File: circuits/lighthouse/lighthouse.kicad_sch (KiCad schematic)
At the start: 5 parts, among them U1 ESP32 CP2102, U3 DCDC_StepUp_SX1308

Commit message: Circuits
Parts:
- added D1, D2, D3, D4: LED, LED_SMD:LED_1206_3216Metric_Pad1.42x1.75mm_HandSolder, symbol Device:LED
- added Q1: S9013, Package_TO_SOT_THT:TO-92_Inline, symbol Transistor_BJT:2N3904
- added R1: 10k, Resistor_SMD:R_1206_3216Metric_Pad1.30x1.75mm_HandSolder, symbol Device:R
- added R2: 20k, Resistor_SMD:R_1206_3216Metric_Pad1.30x1.75mm_HandSolder, symbol Device:R
- added R3, R4, R5, R6: 1k, Resistor_SMD:R_1206_3216Metric_Pad1.30x1.75mm_HandSolder, symbol Device:R
- added R7: 240, LED_SMD:LED_1206_3216Metric_Pad1.42x1.75mm_HandSolder, symbol Device:R
- BT1: footprint Battery:BatteryHolder_MPD_BK-18650-PC2 -> Battery:BatteryHolder_MPD_BH-18650-PC
- U3: renamed from U2; footprint Battery:BatteryHolder_MPD_BH-18650-PC -> YR300:YR300
- renumbered U3 to U2
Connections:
- net GND: now reaches U1.38 (GND), U2.3 (GND)
- net GND: now also Q1.1 (E), R2.2, R3.2, R4.2, R5.2, R6.2
- net 5V: now reaches U1.19 (V5), U2.4 (Vout)
- net 5V: now also U3.1 (3V), R1.1
- net TX: now reaches U3.2 (RX)
- net TX: now also U1.17 (GPIO10__/_S03)
- net RX: now reaches U3.3 (TX)
- net RX: now also U1.16 (GPIO9_/_SO2)
- net at U3.4 (GND): now also Q1.3 (C)
- net RFID_PW: now reaches U1.3 (GPIO36)
- net RFID_PW: now also R7.1
- net PWR_SENSE: now reaches U1.36 (GPIO22)
- net PWR_SENSE: now also R1.2, R2.1
- net MQTT_STS: now reaches U1.4 (GPIO39)
- net MQTT_STS: now also D1.2 (A)
- net WIFI_STS: now reaches U1.5 (GPIO34)
- net WIFI_STS: now also D2.2 (A)
- net SCAN_DETECTED: now reaches U1.6 (GPIO35)
- net SCAN_DETECTED: now also D3.2 (A)
- net ACTIVE_SCAN: now reaches U1.7 (GPIO32)
- net ACTIVE_SCAN: now also D4.2 (A)
- new net: D1.1 (K), R3.1
- new net: Q1.2 (B), R7.2
- new net: D4.1 (K), R6.1
- new net: D2.1 (K), R4.1
- new net: D3.1 (K), R5.1
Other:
- moved on the sheet: CH1, U1, U2, U3

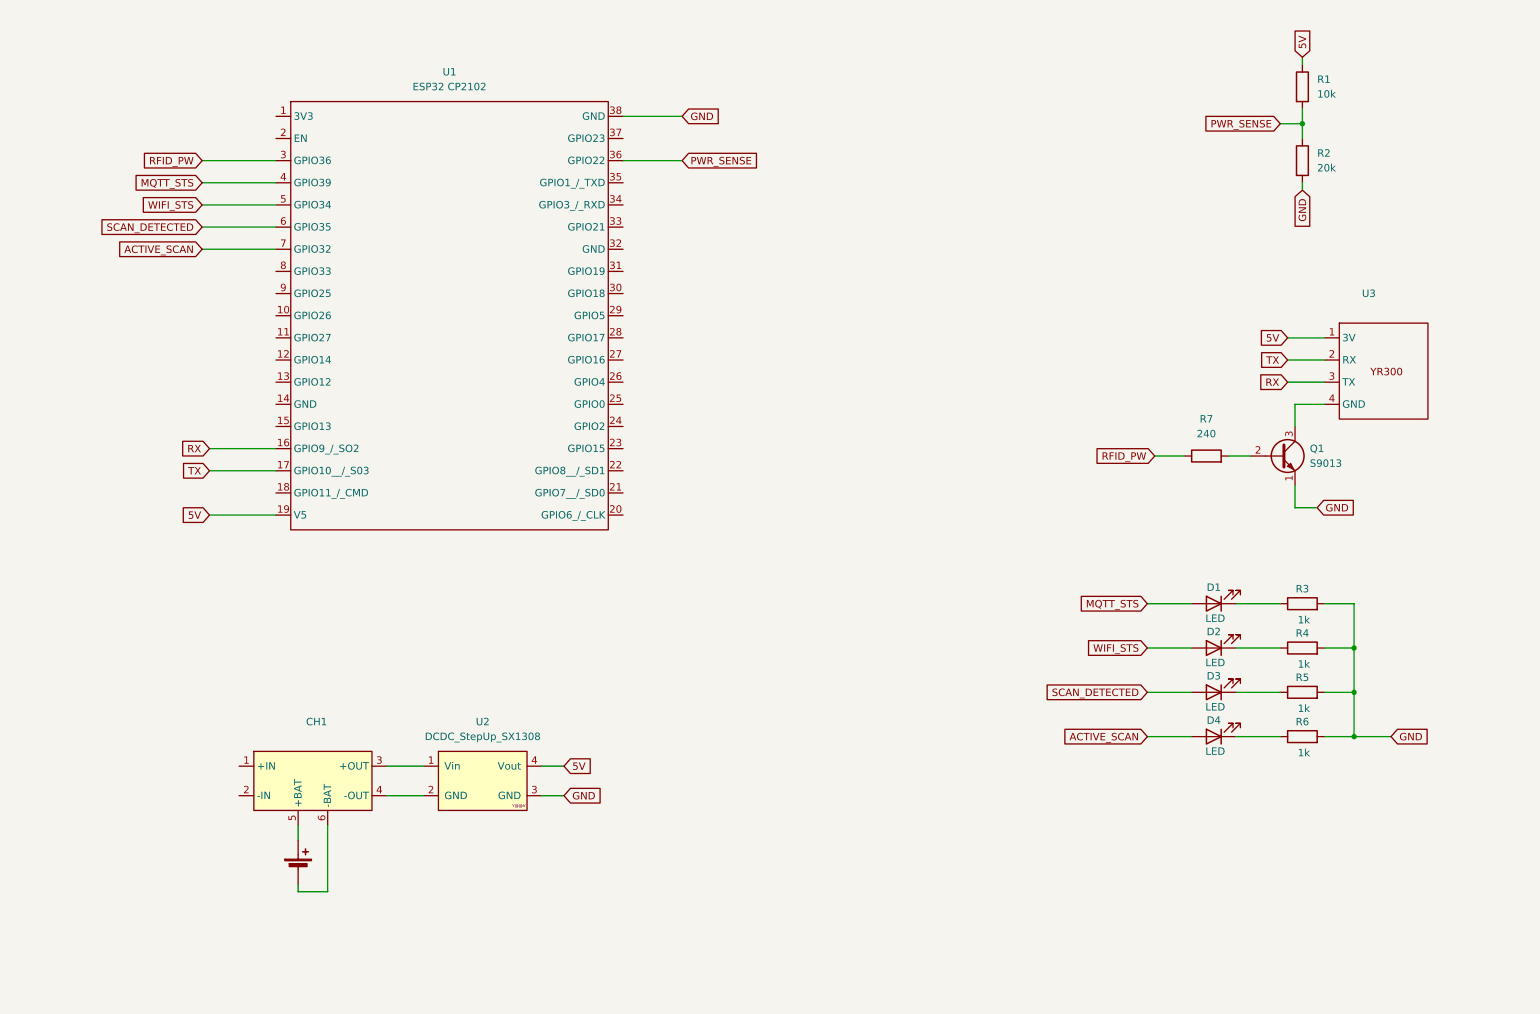
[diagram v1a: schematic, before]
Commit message: Reverse engineered cell charger (component values missing)
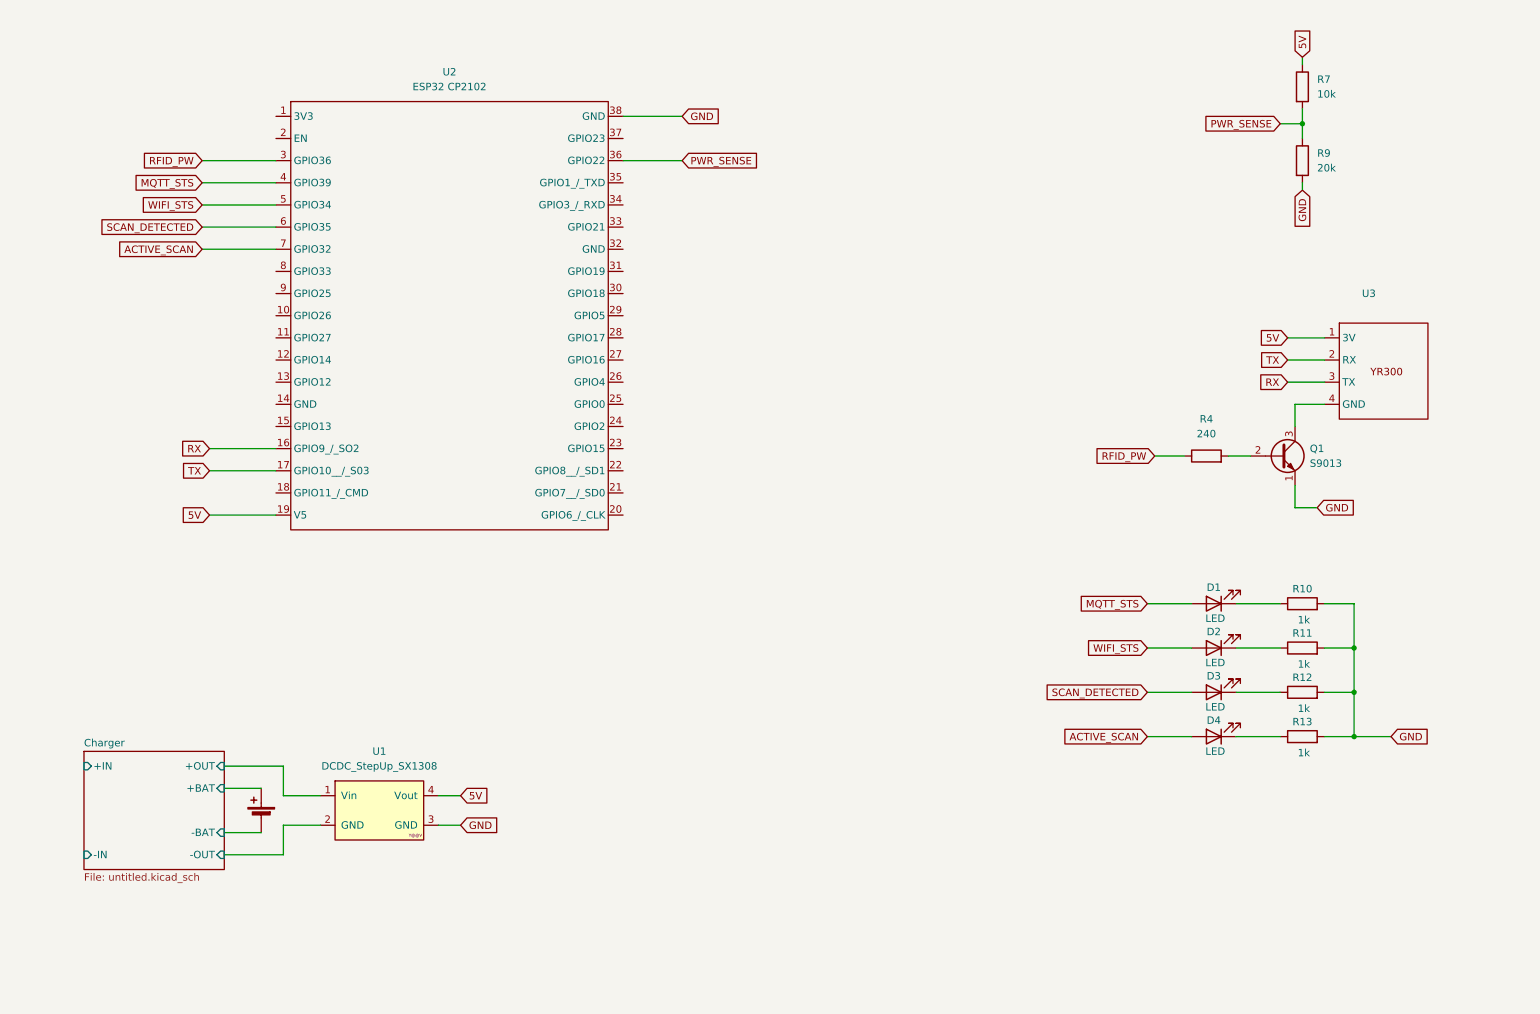
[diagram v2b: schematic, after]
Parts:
- removed CH1: ~, TP4056_Charging_module:TP4056_Charging_Module_Type_C, symbol TP4056_Charging_module:5V-3.3V_MINI_CHARGER_TYPE_C
- renumbered R3 to R10, R4 to R11, R5 to R12, R6 to R13, R7 to R4, R1 to R7, R2 to R9, U2 to U1, U1 to U2
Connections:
- net Charger/+OUT: now reaches U1.1 (Vin)
- net Charger/-OUT: now reaches U1.2 (GND)
- net Charger/+BAT: now reaches BT1.1 (+)
- net Charger/-BAT: now reaches BT1.2 (-)
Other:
- added sheet Charger (untitled.kicad_sch)
- moved on the sheet: U1

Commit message: More circuits
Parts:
- removed U1: DCDC_StepUp_SX1308, SX1308_DCDC_boost:DCDC_StepUp_SX1308, symbol DCDC_StepUp_SX1308:DCDC_StepUp_SX1308
- removed U2: ESP32 CP2102, ESP32:ESP32_38Pin, symbol ESP32:ESP32_38Pin_Symbol
- removed U3: ~, YR300:YR300, symbol YR300:YR300
- added BOOT1, EN1: SW_Push, Button_Switch_SMD:SW_Push_SPST_NO_Alps_SKRK, symbol Switch:SW_Push
- added C10, C11, C12, C13: C, Capacitor_SMD:C_1206_3216Metric_Pad1.33x1.80mm_HandSolder, symbol Device:C
- added D12: D_Schottky, Diode_SMD:D_2114_3652Metric_Pad1.85x3.75mm_HandSolder, symbol Device:D_Schottky
- added D13, D14: LED, LED_SMD:LED_1206_3216Metric_Pad1.42x1.75mm_HandSolder, symbol Device:LED
- added Q4, Q5: SS8050, Package_TO_SOT_SMD:SOT-23, symbol Transistor_BJT:SS8050
- added R20, R21, R22, R25, R26, R27, R30: 10k, Resistor_SMD:R_1206_3216Metric_Pad1.30x1.75mm_HandSolder, symbol Device:R
- added R23, R24, R28, R29: 1k, Resistor_SMD:R_1206_3216Metric_Pad1.30x1.75mm_HandSolder, symbol Device:R
- added U10: CP2102-GMR, CP2102-GMR:QFN28_5X5_SIL, symbol CP2102-GMR:CP2102-GMR
- added U2: AMS1117-3.3, Package_TO_SOT_SMD:SOT-223-3_TabPin2, symbol Regulator_Linear:AMS1117-3.3
- added U7: ESP32-WROOM-32, RF_Module:ESP32-WROOM-32, symbol RF_Module:ESP32-WROOM-32
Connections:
- net 5V: now also U2.3 (VI)
- net ACTIVE_SCAN: now also U7.30 (IO18)
- net GND: now also BOOT1.1, C10.1, C11.2, C12.2, C13.2, D12.2 (A), EN1.1, R22.1, R23.1, R24.1, U10.3 (GND), U2.1 (GND), U7.1 (GND), U7.15 (GND), U7.38 (GND), U7.39 (GND)
- net MQTT_STS: now also R21.2, U7.29 (IO5)
- net RFID_PW: now also U7.33 (IO21)
- net RX: now also U7.27 (IO16)
- net SCAN_DETECTED: now also U7.31 (IO19)
- net TX: now also U7.28 (IO17)
- net WIFI_STS: now also U7.37 (IO23)
- net R300/GND: now reaches Q1.3 (C)
- net PWR_SENSE: no longer names the net of R7.2, R9.1
- net PWR_SENSE: now also U7.36 (IO22)
- new net: R29.2, U10.25 (RXD)
- new net: Q5.1 (B), R26.2
- new net: D13.1 (K), R24.2
- new net: C10.2, U10.6 (VDD)
- new net: R28.2, U10.26 (TXD)
- new net: D14.1 (K), R23.2
- new net: Q4.1 (B), R27.2
- new net 3.3V: C12.1, C13.1, D12.1 (K), D14.2 (A), R20.1, R21.1, R25.1, R30.1, U10.7 (REGIN), U2.2 (VO), U7.2 (VDD)
- new net EN: C11.1, EN1.2, Q5.3 (C), R20.2, U7.3 (EN)
- new net ESP24: D13.2 (A), R22.2, U7.24 (IO2)
- new net ESP25: BOOT1.2, Q4.3 (C), R25.2, U7.25 (IO0)
- new net ESP34: R29.1, R30.2, U7.34 (RXD0/IO3)
- new net ESP35: R28.1, U7.35 (TXD0/IO1)
- new net MP24: Q5.2 (E), R27.1, U10.24 (RTS)
- new net MP28: Q4.2 (E), R26.1, U10.28 (DTR)
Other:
- added sheet R300 (r300.kicad_sch)
- added sheet Step-Up DC-DC (setp_up_dc_dc.kicad_sch)
- sheet Charger: file untitled.kicad_sch -> charger.kicad_sch
- moved on the sheet: D1, D2, D3, D4, Q1, R10, R11, R12, R13, R4, R7, R9

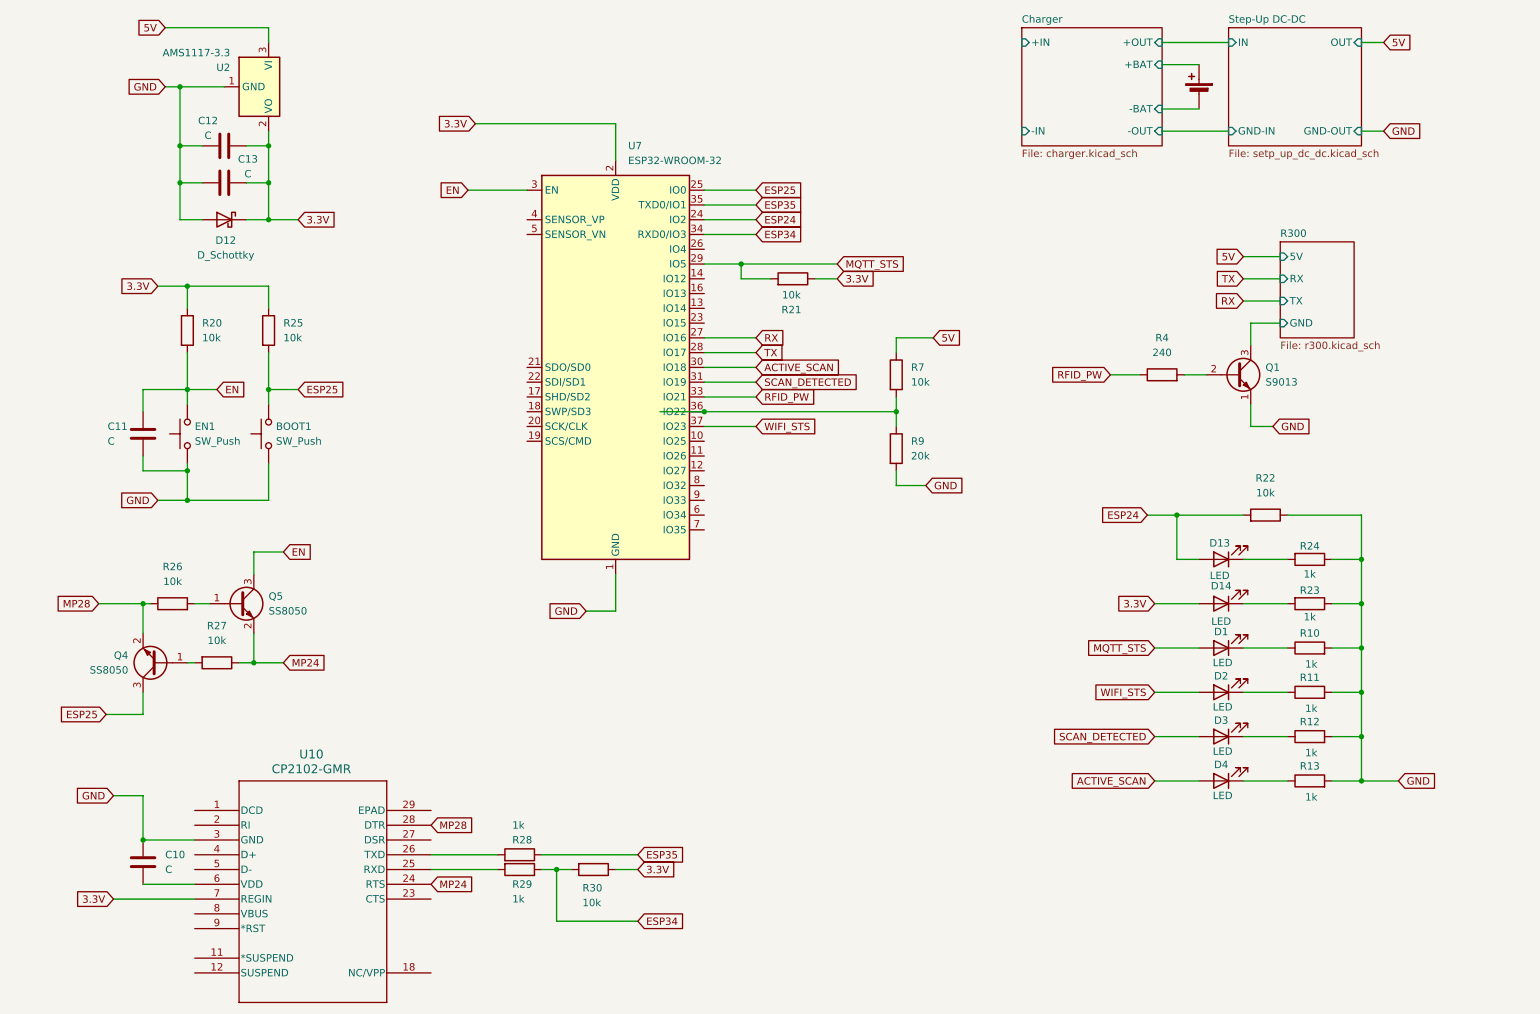
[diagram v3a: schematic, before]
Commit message: The circuit now has all the values in place
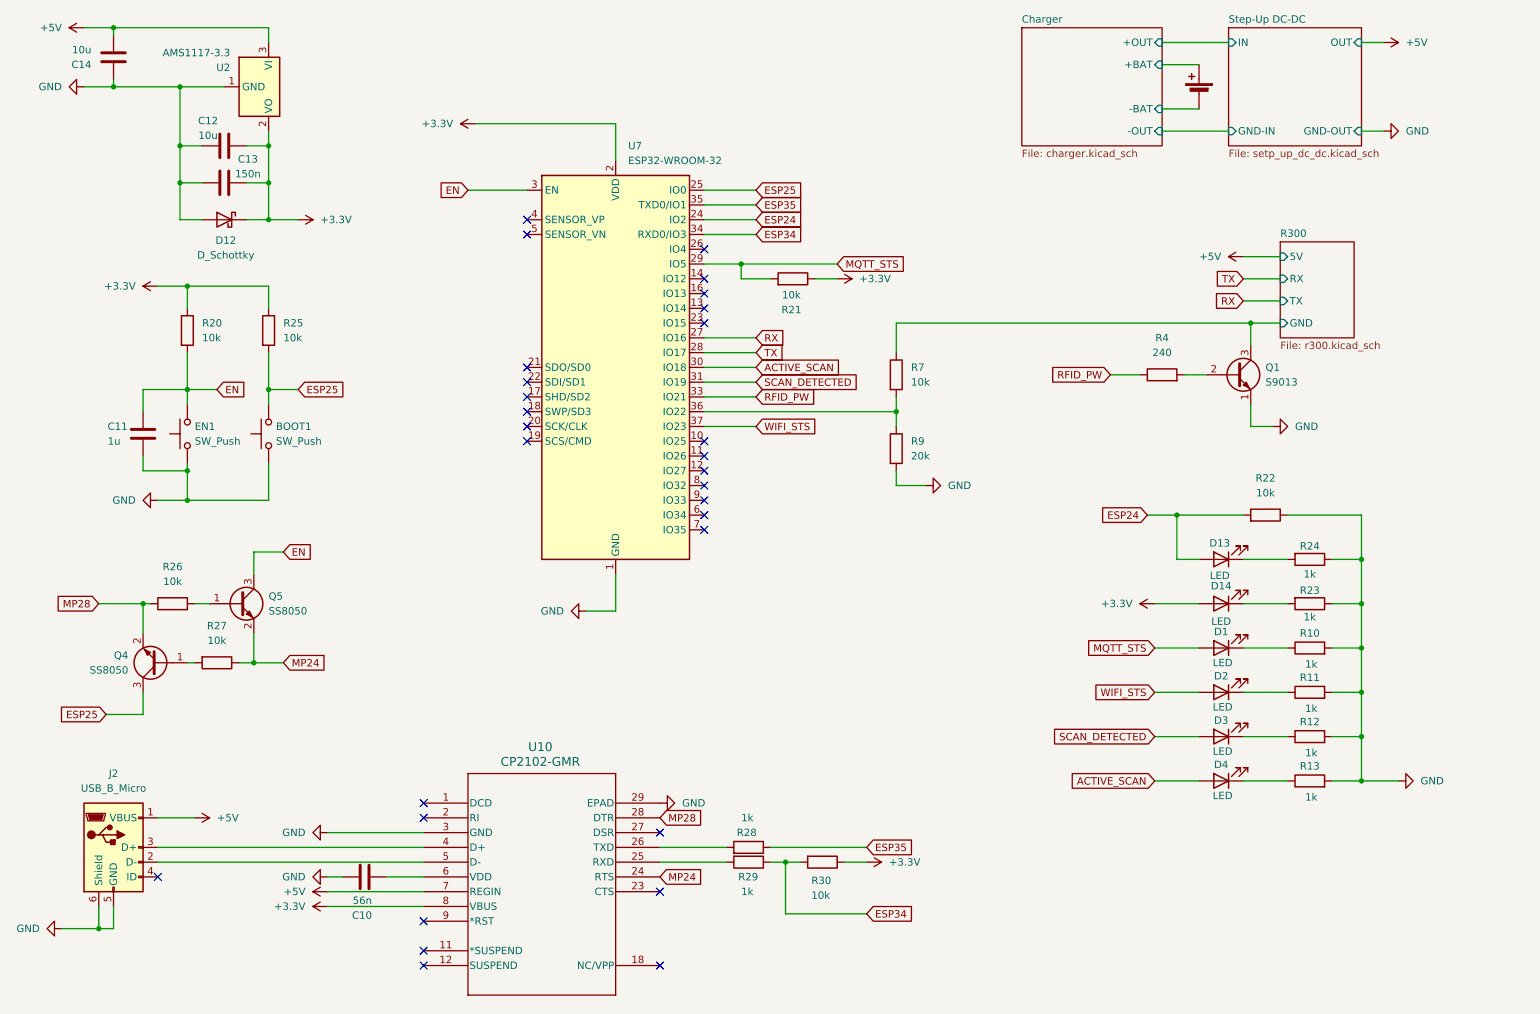
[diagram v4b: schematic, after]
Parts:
- added C14: 10u, Capacitor_SMD:C_1206_3216Metric_Pad1.33x1.80mm_HandSolder, symbol Device:C
- added J2: USB_B_Micro, Connector_USB:USB_Micro-B_Amphenol_10103594-0001LF_Horizontal, symbol Connector:USB_B_Micro
- C10: value C -> 56n
- C11: value C -> 1u
- C12: value C -> 10u
- C13: value C -> 150n
- R4: footprint LED_SMD:LED_1206_3216Metric_Pad1.42x1.75mm_HandSolder -> Resistor_SMD:R_1206_3216Metric_Pad1.30x1.75mm_HandSolder
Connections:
- net GND: now also U10.29 (EPAD), C14.1, J2.5 (GND), J2.6 (Shield)
- net R300/GND: now also R7.1
- net at U10.4 (D+): now also J2.3 (D+)
- net at U10.5 (D-): now also J2.2 (D-)
- net +3.3V: now reaches U10.8 (VBUS)
- net +3.3V: now also C12.1, C13.1, D12.1 (K), D14.2 (A), R20.1, R21.1, R25.1, R30.1, U2.2 (VO), U7.2 (VDD)
- removed net 3.3V: C12.1, C13.1, D12.1 (K), D14.2 (A), R20.1, R21.1, R25.1, R30.1, U10.7 (REGIN), U2.2 (VO), U7.2 (VDD)
- net 5V renamed +5V
- net +5V: now also U10.7 (REGIN), C14.2, J2.1 (VBUS); no longer R7.1
- no-connect marks 0 -> 29
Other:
- sheet Charger ports: added none; removed +IN, -IN
- moved on the sheet: C10, R28, R29, R30, U10
